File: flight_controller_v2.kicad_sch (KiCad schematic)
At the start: 0 parts

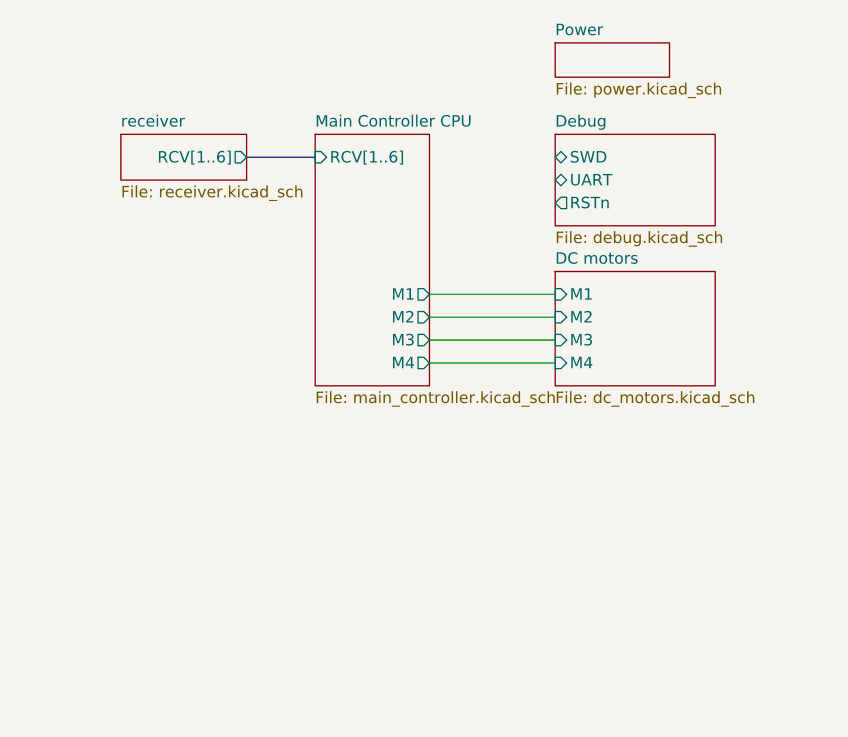
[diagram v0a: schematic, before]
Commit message: Add QSPI flash
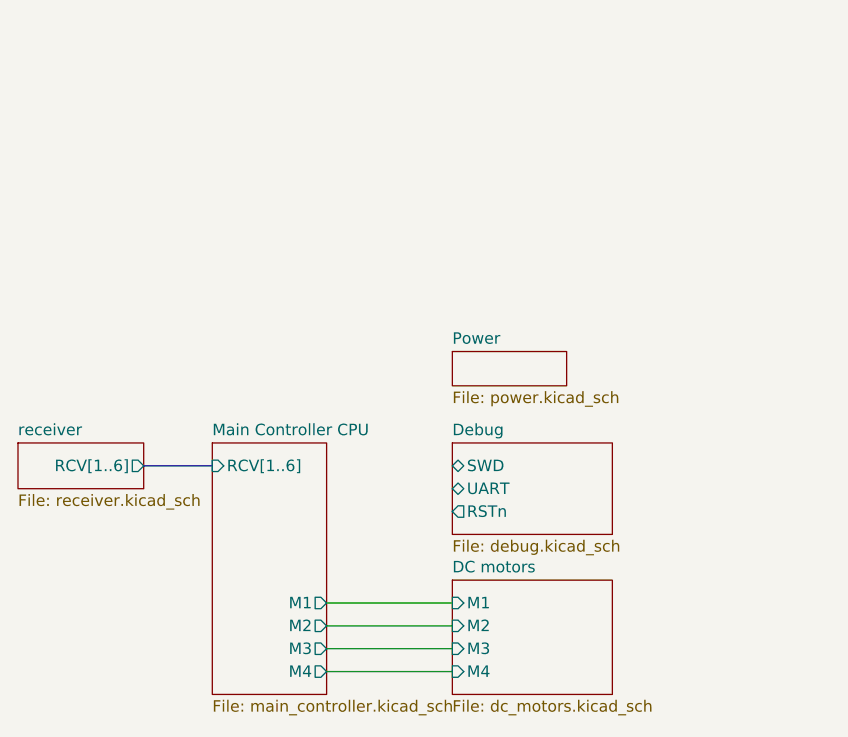
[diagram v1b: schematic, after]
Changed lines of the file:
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@@
 (kicad_sch (version 20211123) (generator eeschema)
   (paper "A4")
-  (wire (pts (xy 143.51 83.82) (xy 157.48 83.82))
-    (stroke (width 0) (type default) (color 0 0 0 0))
-  )
-  (wire (pts (xy 143.51 86.36) (xy 157.48 86.36))
-    (stroke (width 0) (type default) (color 0 0 0 0))
-  )
-  (bus (pts (xy 123.19 63.5) (xy 130.81 63.5))
-    (stroke (width 0) (type default) (color 0 0 0 0))
-  )
-  (wire (pts (xy 143.51 81.28) (xy 157.48 81.28))
-    (stroke (width 0) (type default) (color 0 0 0 0))
-  )
-  (wire (pts (xy 143.51 78.74) (xy 157.48 78.74))
-    (stroke (width 0) (type default) (color 0 0 0 0))
-  )
-  (sheet (at 130.81 60.96) (size 12.7 27.94) (fields_autoplaced)
-    (stroke (width 0) (type solid) (color 0 0 0 0))
-    (fill (color 0 0 0 0.0000))
-    (property "Sheet name" "Main Controller CPU" (id 0) (at 130.81 60.2484 0)
-      (effects (font (size 1.27 1.27)) (justify left bottom))
-    )
-    (property "Sheet file" "main_controller.kicad_sch" (id 1) (at 130.81 89.4846 0)
-      (effects (font (size 1.27 1.27)) (justify left top))
-    )
-    (pin "M1" output (at 143.51 78.74 0)
-      (effects (font (size 1.27 1.27)) (justify right))
-    )
-    (pin "M2" output (at 143.51 81.28 0)
-      (effects (font (size 1.27 1.27)) (justify right))
-    )
-    (pin "M3" output (at 143.51 83.82 0)
-      (effects (font (size 1.27 1.27)) (justify right))
-    )
-    (pin "M4" output (at 143.51 86.36 0)
-      (effects (font (size 1.27 1.27)) (justify right))
-    )
-    (pin "RCV[1..6]" input (at 130.81 63.5 180)
-      (effects (font (size 1.27 1.27)) (justify left))
-    )
-  )
-  (sheet (at 157.48 76.2) (size 17.78 12.7) (fields_autoplaced)
-    (stroke (width 0) (type solid) (color 0 0 0 0))
-    (fill (color 0 0 0 0.0000))
-    (property "Sheet name" "DC motors" (id 0) (at 157.48 75.4884 0)
-      (effects (font (size 1.27 1.27)) (justify left bottom))
-    )
-    (property "Sheet file" "dc_motors.kicad_sch" (id 1) (at 157.48 89.4846 0)
-      (effects (font (size 1.27 1.27)) (justify left top))
-    )
-    (pin "M1" input (at 157.48 78.74 180)
-      (effects (font (size 1.27 1.27)) (justify left))
-    )
-    (pin "M2" input (at 157.48 81.28 180)
-      (effects (font (size 1.27 1.27)) (justify left))
-    )
-    (pin "M3" input (at 157.48 83.82 180)
-      (effects (font (size 1.27 1.27)) (justify left))
-    )
-    (pin "M4" input (at 157.48 86.36 180)
-      (effects (font (size 1.27 1.27)) (justify left))
-    )
-  )
-  (sheet (at 157.48 60.96) (size 17.78 10.16) (fields_autoplaced)
-    (stroke (width 0) (type solid) (color 0 0 0 0))
-    (fill (color 0 0 0 0.0000))
-    (property "Sheet name" "Debug" (id 0) (at 157.48 60.2484 0)
-      (effects (font (size 1.27 1.27)) (justify left bottom))
-    )
-    (property "Sheet file" "debug.kicad_sch" (id 1) (at 157.48 71.7046 0)
-      (effects (font (size 1.27 1.27)) (justify left top))
-    )
-    (pin "SWD" bidirectional (at 157.48 63.5 180)
-      (effects (font (size 1.27 1.27)) (justify left))
-    )
-    (pin "UART" bidirectional (at 157.48 66.04 180)
-      (effects (font (size 1.27 1.27)) (justify left))
-    )
-    (pin "RSTn" output (at 157.48 68.58 180)
-      (effects (font (size 1.27 1.27)) (justify left))
-    )
-  )
-  (sheet (at 157.48 50.8) (size 12.7 3.81) (fields_autoplaced)
-    (stroke (width 0) (type solid) (color 0 0 0 0))
-    (fill (color 0 0 0 0.0000))
-    (property "Sheet name" "Power" (id 0) (at 157.48 50.0884 0)
-      (effects (font (size 1.27 1.27)) (justify left bottom))
-    )
-    (property "Sheet file" "power.kicad_sch" (id 1) (at 157.48 55.1946 0)
-      (effects (font (size 1.27 1.27)) (justify left top))
-    )
-  )
-  (sheet (at 109.22 60.96) (size 13.97 5.08) (fields_autoplaced)
-    (stroke (width 0) (type solid) (color 0 0 0 0))
-    (fill (color 0 0 0 0.0000))
-    (property "Sheet name" "receiver" (id 0) (at 109.22 60.2484 0)
-      (effects (font (size 1.27 1.27)) (justify left bottom))
-    )
-    (property "Sheet file" "receiver.kicad_sch" (id 1) (at 109.22 66.6246 0)
-      (effects (font (size 1.27 1.27)) (justify left top))
-    )
-    (pin "RCV[1..6]" output (at 123.19 63.5 0)
+  (wire (pts (xy 132.08 118.11) (xy 146.05 118.11))
+    (stroke (width 0) (type default) (color 0 0 0 0))
+  )
+  (wire (pts (xy 132.08 120.65) (xy 146.05 120.65))
+    (stroke (width 0) (type default) (color 0 0 0 0))
+  )
+  (bus (pts (xy 111.76 97.79) (xy 119.38 97.79))
+    (stroke (width 0) (type default) (color 0 0 0 0))
+  )
+  (wire (pts (xy 132.08 115.57) (xy 146.05 115.57))
+    (stroke (width 0) (type default) (color 0 0 0 0))
+  )
+  (wire (pts (xy 132.08 113.03) (xy 146.05 113.03))
+    (stroke (width 0) (type default) (color 0 0 0 0))
+  )
+  (sheet (at 119.38 95.25) (size 12.7 27.94) (fields_autoplaced)
+    (stroke (width 0) (type solid) (color 0 0 0 0))
+    (fill (color 0 0 0 0.0000))
+    (property "Sheet name" "Main Controller CPU" (id 0) (at 119.38 94.5384 0)
+      (effects (font (size 1.27 1.27)) (justify left bottom))
+    )
+    (property "Sheet file" "main_controller.kicad_sch" (id 1) (at 119.38 123.7746 0)
+      (effects (font (size 1.27 1.27)) (justify left top))
+    )
+    (pin "M1" output (at 132.08 113.03 0)
+      (effects (font (size 1.27 1.27)) (justify right))
+    )
+    (pin "M2" output (at 132.08 115.57 0)
+      (effects (font (size 1.27 1.27)) (justify right))
+    )
+    (pin "M3" output (at 132.08 118.11 0)
+      (effects (font (size 1.27 1.27)) (justify right))
+    )
+    (pin "M4" output (at 132.08 120.65 0)
+      (effects (font (size 1.27 1.27)) (justify right))
+    )
+    (pin "RCV[1..6]" input (at 119.38 97.79 180)
+      (effects (font (size 1.27 1.27)) (justify left))
+    )
+  )
+  (sheet (at 146.05 110.49) (size 17.78 12.7) (fields_autoplaced)
+    (stroke (width 0) (type solid) (color 0 0 0 0))
+    (fill (color 0 0 0 0.0000))
+    (property "Sheet name" "DC motors" (id 0) (at 146.05 109.7784 0)
+      (effects (font (size 1.27 1.27)) (justify left bottom))
+    )
+    (property "Sheet file" "dc_motors.kicad_sch" (id 1) (at 146.05 123.7746 0)
+      (effects (font (size 1.27 1.27)) (justify left top))
+    )
+    (pin "M1" input (at 146.05 113.03 180)
+      (effects (font (size 1.27 1.27)) (justify left))
+    )
+    (pin "M2" input (at 146.05 115.57 180)
+      (effects (font (size 1.27 1.27)) (justify left))
+    )
+    (pin "M3" input (at 146.05 118.11 180)
+      (effects (font (size 1.27 1.27)) (justify left))
+    )
+    (pin "M4" input (at 146.05 120.65 180)
+      (effects (font (size 1.27 1.27)) (justify left))
+    )
+  )
+  (sheet (at 146.05 95.25) (size 17.78 10.16) (fields_autoplaced)
+    (stroke (width 0) (type solid) (color 0 0 0 0))
+    (fill (color 0 0 0 0.0000))
+    (property "Sheet name" "Debug" (id 0) (at 146.05 94.5384 0)
+      (effects (font (size 1.27 1.27)) (justify left bottom))
+    )
+    (property "Sheet file" "debug.kicad_sch" (id 1) (at 146.05 105.9946 0)
+      (effects (font (size 1.27 1.27)) (justify left top))
+    )
+    (pin "SWD" bidirectional (at 146.05 97.79 180)
+      (effects (font (size 1.27 1.27)) (justify left))
+    )
+    (pin "UART" bidirectional (at 146.05 100.33 180)
+      (effects (font (size 1.27 1.27)) (justify left))
+    )
+    (pin "RSTn" output (at 146.05 102.87 180)
+      (effects (font (size 1.27 1.27)) (justify left))
+    )
+  )
+  (sheet (at 146.05 85.09) (size 12.7 3.81) (fields_autoplaced)
+    (stroke (width 0) (type solid) (color 0 0 0 0))
+    (fill (color 0 0 0 0.0000))
+    (property "Sheet name" "Power" (id 0) (at 146.05 84.3784 0)
+      (effects (font (size 1.27 1.27)) (justify left bottom))
+    )
+    (property "Sheet file" "power.kicad_sch" (id 1) (at 146.05 89.4846 0)
+      (effects (font (size 1.27 1.27)) (justify left top))
+    )
+  )
+  (sheet (at 97.79 95.25) (size 13.97 5.08) (fields_autoplaced)
+    (stroke (width 0) (type solid) (color 0 0 0 0))
+    (fill (color 0 0 0 0.0000))
+    (property "Sheet name" "receiver" (id 0) (at 97.79 94.5384 0)
+      (effects (font (size 1.27 1.27)) (justify left bottom))
+    )
+    (property "Sheet file" "receiver.kicad_sch" (id 1) (at 97.79 100.9146 0)
+      (effects (font (size 1.27 1.27)) (justify left top))
+    )
+    (pin "RCV[1..6]" output (at 111.76 97.79 0)
       (effects (font (size 1.27 1.27)) (justify right))
     )
@@
       (reference "#PWR0105") (unit 1) (value "GND") (footprint "")
     )
+    (path "/00000000-0000-0000-0000-0000623a7d84/25ffdd34-1e23-49fd-83d1-8a8d46bab666"
+      (reference "#PWR?") (unit 1) (value "+2V8") (footprint "")
+    )
+    (path "/00000000-0000-0000-0000-0000623a7d84/79949015-ec1d-41ce-a46d-1089fdaaa62a"
+      (reference "#PWR?") (unit 1) (value "GND") (footprint "")
+    )
     (path "/00000000-0000-0000-0000-000063b0677d/00000000-0000-0000-0000-000063b1aa8e"
       (reference "C1") (unit 1) (value "1uF") (footprint "Capacitor_SMD:C_0402_1005Metric")
@@
       (reference "C2") (unit 1) (value "1uF") (footprint "Capacitor_SMD:C_0402_1005Metric")
     )
+    (path "/00000000-0000-0000-0000-0000623a7d84/4d4b6209-a96d-4ebc-aa21-d2d153d10039"
+      (reference "C?") (unit 1) (value "100n") (footprint "")
+    )
     (path "/00000000-0000-0000-0000-000063ad176a/00000000-0000-0000-0000-000063c6b6e0"
       (reference "D1") (unit 1) (value "BAT54W-HG3-08") (footprint "Diode_SMD:D_SOD-123")
@@
       (reference "U2") (unit 1) (value "RP2040") (footprint "rp2040:RP2040")
     )
-  )
+    (path "/00000000-0000-0000-0000-0000623a7d84/f006ac40-8ebe-4422-a6f4-50c5c2569bba"
+      (reference "U?") (unit 1) (value "W25Q32JVSS") (footprint "Package_SO:SOIC-8_5.23x5.23mm_P1.27mm")
+    )
+  )
